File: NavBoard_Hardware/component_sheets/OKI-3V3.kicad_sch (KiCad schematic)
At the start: 4 parts, among them U4 OKI-3V3

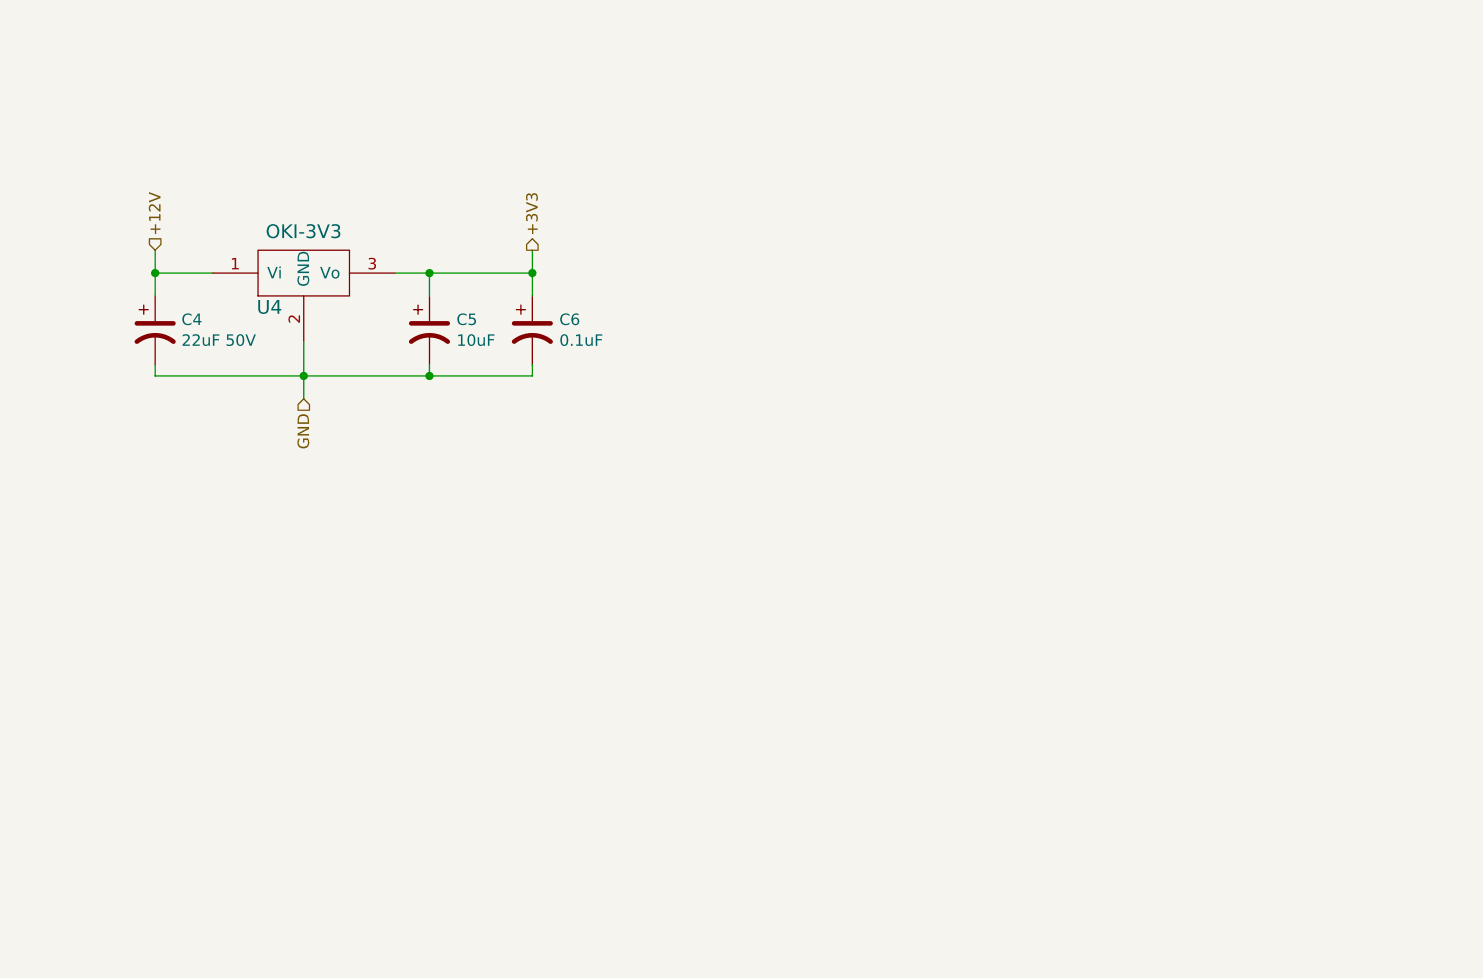
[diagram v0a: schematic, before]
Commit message: Added Information To Voltage Regulator Component Sheets, Improved Schematic Review 1 Powerpoint
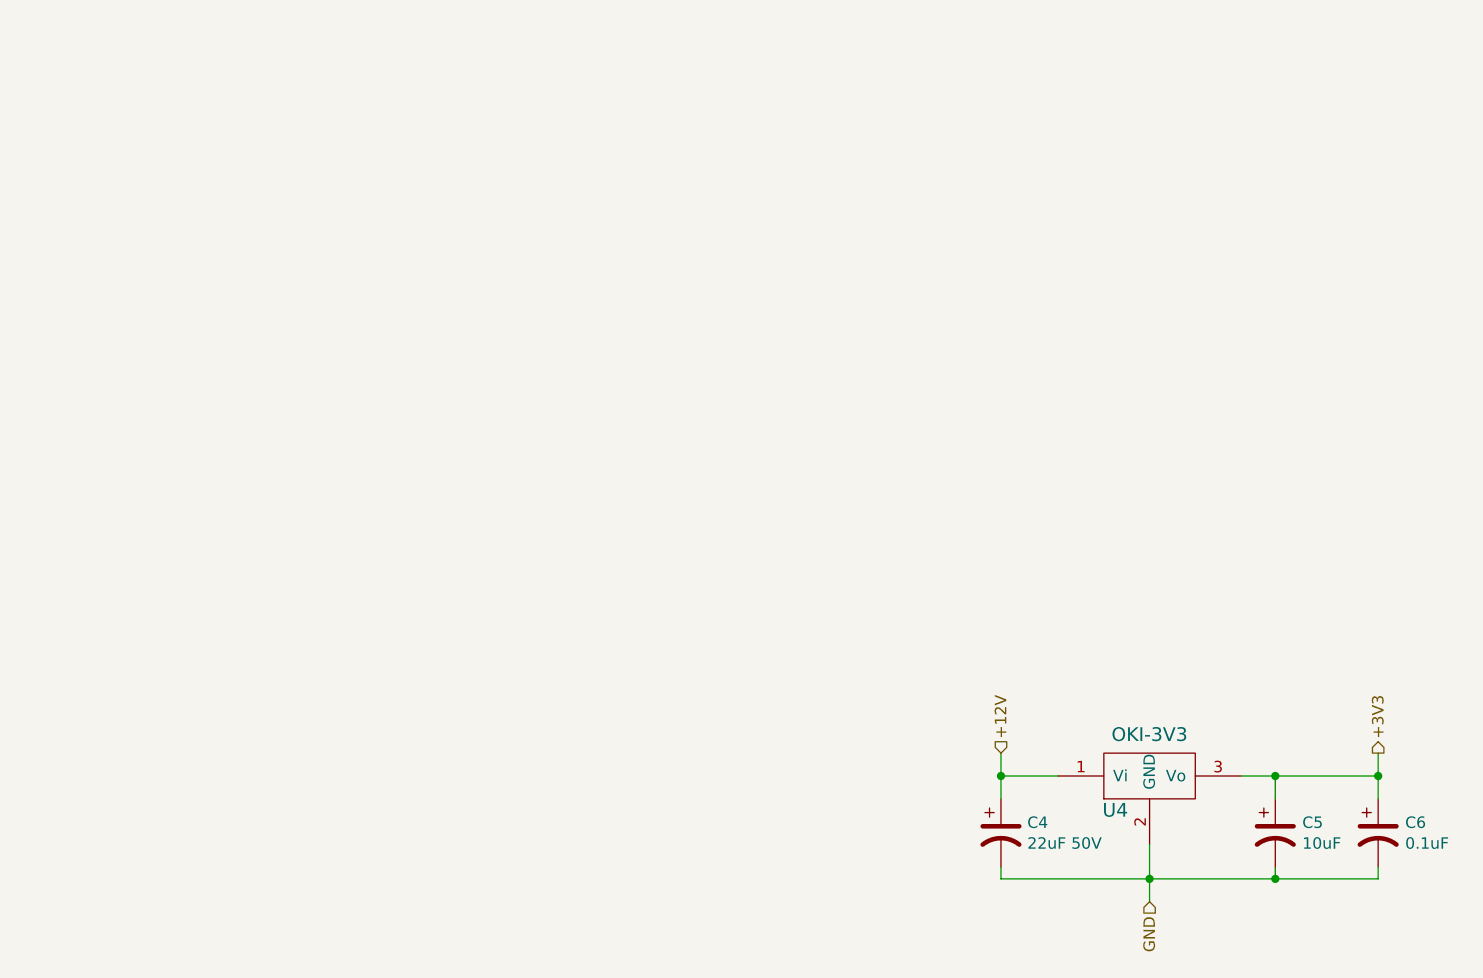
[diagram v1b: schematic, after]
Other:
- company: (none) -> Missouri S&T Mars Rover Design Team
- title: (none) -> OKI 3V3 Voltage Regulator
- moved on the sheet: C4, C5, C6, U4
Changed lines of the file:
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@@
 (kicad_sch (version 20211123) (generator eeschema)
   (paper "A4")
-  (junction (at 115.57 90.17) (diameter 0) (color 0 0 0 0)
+  (title_block
+    (title "OKI 3V3 Voltage Regulator")
+    (date "2022-09-17")
+    (rev "2, 2023")
+    (company "Missouri S&T Mars Rover Design Team")
+    (comment 1 "OKI 3V3 Voltage Regulator")
+    (comment 2 "Provides Stable 3V3 From 12V")
   )
-  (junction (at 157.48 90.17) (diameter 0) (color 0 0 0 0)
+  (junction (at 209.55 146.05) (diameter 0) (color 0 0 0 0)
   )
-  (junction (at 146.05 90.17) (diameter 0) (color 0 0 0 0)
+  (junction (at 251.46 146.05) (diameter 0) (color 0 0 0 0)
   )
-  (junction (at 146.05 101.6) (diameter 0) (color 0 0 0 0)
+  (junction (at 240.03 146.05) (diameter 0) (color 0 0 0 0)
   )
-  (junction (at 132.08 101.6) (diameter 0) (color 0 0 0 0)
+  (junction (at 240.03 157.48) (diameter 0) (color 0 0 0 0)
   )
-  (wire (pts (xy 146.05 101.6) (xy 157.48 101.6))
+  (junction (at 226.06 157.48) (diameter 0) (color 0 0 0 0)
+  )
+  (wire (pts (xy 240.03 157.48) (xy 251.46 157.48))
     (stroke (width 0) (type default) (color 0 0 0 0))
   )
-  (wire (pts (xy 132.08 101.6) (xy 146.05 101.6))
+  (wire (pts (xy 226.06 157.48) (xy 240.03 157.48))
     (stroke (width 0) (type default) (color 0 0 0 0))
   )
-  (wire (pts (xy 121.92 90.17) (xy 115.57 90.17))
+  (wire (pts (xy 215.9 146.05) (xy 209.55 146.05))
     (stroke (width 0) (type default) (color 0 0 0 0))
   )
-  (wire (pts (xy 146.05 101.6) (xy 146.05 100.33))
+  (wire (pts (xy 240.03 157.48) (xy 240.03 156.21))
     (stroke (width 0) (type default) (color 0 0 0 0))
   )
-  (wire (pts (xy 146.05 90.17) (xy 157.48 90.17))
+  (wire (pts (xy 240.03 146.05) (xy 251.46 146.05))
     (stroke (width 0) (type default) (color 0 0 0 0))
   )
-  (wire (pts (xy 132.08 97.79) (xy 132.08 101.6))
+  (wire (pts (xy 226.06 153.67) (xy 226.06 157.48))
     (stroke (width 0) (type default) (color 0 0 0 0))
   )
-  (wire (pts (xy 157.48 92.71) (xy 157.48 90.17))
+  (wire (pts (xy 251.46 148.59) (xy 251.46 146.05))
     (stroke (width 0) (type default) (color 0 0 0 0))
   )
-  (wire (pts (xy 157.48 90.17) (xy 157.48 87.63))
+  (wire (pts (xy 251.46 146.05) (xy 251.46 143.51))
     (stroke (width 0) (type default) (color 0 0 0 0))
   )
-  (wire (pts (xy 115.57 87.63) (xy 115.57 90.17))
+  (wire (pts (xy 209.55 143.51) (xy 209.55 146.05))
     (stroke (width 0) (type default) (color 0 0 0 0))
   )
-  (wire (pts (xy 142.24 90.17) (xy 146.05 90.17))
+  (wire (pts (xy 236.22 146.05) (xy 240.03 146.05))
     (stroke (width 0) (type default) (color 0 0 0 0))
   )
-  (wire (pts (xy 115.57 90.17) (xy 115.57 92.71))
+  (wire (pts (xy 209.55 146.05) (xy 209.55 148.59))
     (stroke (width 0) (type default) (color 0 0 0 0))
   )
-  (wire (pts (xy 115.57 101.6) (xy 132.08 101.6))
+  (wire (pts (xy 209.55 157.48) (xy 226.06 157.48))
     (stroke (width 0) (type default) (color 0 0 0 0))
   )
-  (wire (pts (xy 132.08 101.6) (xy 132.08 104.14))
+  (wire (pts (xy 226.06 157.48) (xy 226.06 160.02))
     (stroke (width 0) (type default) (color 0 0 0 0))
   )
-  (wire (pts (xy 146.05 92.71) (xy 146.05 90.17))
+  (wire (pts (xy 240.03 148.59) (xy 240.03 146.05))
     (stroke (width 0) (type default) (color 0 0 0 0))
   )
-  (wire (pts (xy 157.48 101.6) (xy 157.48 100.33))
+  (wire (pts (xy 251.46 157.48) (xy 251.46 156.21))
     (stroke (width 0) (type default) (color 0 0 0 0))
   )
-  (wire (pts (xy 115.57 100.33) (xy 115.57 101.6))
+  (wire (pts (xy 209.55 156.21) (xy 209.55 157.48))
     (stroke (width 0) (type default) (color 0 0 0 0))
   )
-  (hierarchical_label "GND" (shape input) (at 132.08 104.14 270)
+  (hierarchical_label "GND" (shape input) (at 226.06 160.02 270)
     (effects (font (size 1.27 1.27)) (justify right))
   )
-  (hierarchical_label "+3V3" (shape output) (at 157.48 87.63 90)
+  (hierarchical_label "+3V3" (shape output) (at 251.46 143.51 90)
     (effects (font (size 1.27 1.27)) (justify left))
   )
-  (hierarchical_label "+12V" (shape input) (at 115.57 87.63 90)
+  (hierarchical_label "+12V" (shape input) (at 209.55 143.51 90)
     (effects (font (size 1.27 1.27)) (justify left))
   )
-  (symbol (lib_id "MRDT_Devices:OKI") (at 127 92.71 0) (unit 1)
+  (symbol (lib_id "MRDT_Devices:OKI") (at 220.98 148.59 0) (unit 1)
     (in_bom yes) (on_board yes)
-    (property "Reference" "U4" (id 0) (at 128.27 93.98 0)
+    (property "Reference" "U4" (id 0) (at 222.25 149.86 0)
       (effects (font (size 1.524 1.524)))
     )
-    (property "Value" "OKI-3V3" (id 1) (at 132.08 85.5726 0)
+    (property "Value" "OKI-3V3" (id 1) (at 226.06 141.4526 0)
       (effects (font (size 1.524 1.524)))
     )
-    (property "Footprint" "MRDT_Devices:OKI_Horizontal" (id 2) (at 121.92 95.25 0)
+    (property "Footprint" "MRDT_Devices:OKI_Horizontal" (id 2) (at 215.9 151.13 0)
       (effects (font (size 1.524 1.524)) hide)
     )
-    (property "Datasheet" "" (id 3) (at 121.92 95.25 0)
+    (property "Datasheet" "" (id 3) (at 215.9 151.13 0)
       (effects (font (size 1.524 1.524)) hide)
     )
@@
     (pin "3")
   )
-  (symbol (lib_id "Device:C_Polarized_US") (at 115.57 96.52 0) (unit 1)
+  (symbol (lib_id "Device:C_Polarized_US") (at 209.55 152.4 0) (unit 1)
     (in_bom yes) (on_board yes)
-    (property "Reference" "C4" (id 0) (at 118.491 95.3516 0)
+    (property "Reference" "C4" (id 0) (at 212.471 151.2316 0)
       (effects (font (size 1.27 1.27)) (justify left))
     )
-    (property "Value" "22uF 50V" (id 1) (at 118.491 97.663 0)
+    (property "Value" "22uF 50V" (id 1) (at 212.471 153.543 0)
       (effects (font (size 1.27 1.27)) (justify left))
     )
-    (property "Footprint" "Capacitor_THT:CP_Radial_D6.3mm_P2.50mm" (id 2) (at 115.57 96.52 0)
+    (property "Footprint" "Capacitor_THT:CP_Radial_D6.3mm_P2.50mm" (id 2) (at 209.55 152.4 0)
       (effects (font (size 1.27 1.27)) hide)
     )
-    (property "Datasheet" "~" (id 3) (at 115.57 96.52 0)
+    (property "Datasheet" "~" (id 3) (at 209.55 152.4 0)
       (effects (font (size 1.27 1.27)) hide)
     )
@@
     (pin "2")
   )
-  (symbol (lib_id "Device:C_Polarized_US") (at 157.48 96.52 0) (unit 1)
+  (symbol (lib_id "Device:C_Polarized_US") (at 251.46 152.4 0) (unit 1)
     (in_bom yes) (on_board yes)
-    (property "Reference" "C6" (id 0) (at 160.4772 95.3516 0)
+    (property "Reference" "C6" (id 0) (at 254.4572 151.2316 0)
       (effects (font (size 1.27 1.27)) (justify left))
     )
-    (property "Value" "0.1uF" (id 1) (at 160.4772 97.663 0)
+    (property "Value" "0.1uF" (id 1) (at 254.4572 153.543 0)
       (effects (font (size 1.27 1.27)) (justify left))
     )
-    (property "Footprint" "Capacitor_SMD:C_0603_1608Metric_Pad1.08x0.95mm_HandSolder" (id 2) (at 157.48 96.52 0)
+    (property "Footprint" "Capacitor_SMD:C_0603_1608Metric_Pad1.08x0.95mm_HandSolder" (id 2) (at 251.46 152.4 0)
       (effects (font (size 1.27 1.27)) hide)
     )
-    (property "Datasheet" "~" (id 3) (at 157.48 96.52 0)
+    (property "Datasheet" "~" (id 3) (at 251.46 152.4 0)
       (effects (font (size 1.27 1.27)) hide)
     )
@@
     (pin "2")
   )
-  (symbol (lib_id "Device:C_Polarized_US") (at 146.05 96.52 0) (unit 1)
+  (symbol (lib_id "Device:C_Polarized_US") (at 240.03 152.4 0) (unit 1)
     (in_bom yes) (on_board yes)
-    (property "Reference" "C5" (id 0) (at 149.0472 95.3516 0)
+    (property "Reference" "C5" (id 0) (at 243.0272 151.2316 0)
       (effects (font (size 1.27 1.27)) (justify left))
     )
-    (property "Value" "10uF" (id 1) (at 149.0472 97.663 0)
+    (property "Value" "10uF" (id 1) (at 243.0272 153.543 0)
       (effects (font (size 1.27 1.27)) (justify left))
     )
-    (property "Footprint" "Capacitor_SMD:C_0603_1608Metric_Pad1.08x0.95mm_HandSolder" (id 2) (at 146.05 96.52 0)
+    (property "Footprint" "Capacitor_SMD:C_0603_1608Metric_Pad1.08x0.95mm_HandSolder" (id 2) (at 240.03 152.4 0)
       (effects (font (size 1.27 1.27)) hide)
     )
-    (property "Datasheet" "~" (id 3) (at 146.05 96.52 0)
+    (property "Datasheet" "~" (id 3) (at 240.03 152.4 0)
       (effects (font (size 1.27 1.27)) hide)
     )

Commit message: Updated sheet title info
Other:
- company: Missouri S&T Mars Rover Design Team -> Thomas Francois, Katherine Dunlap, Missouri S&T Mars Rover Design Team
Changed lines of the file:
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@@
     (date "2022-09-17")
     (rev "2, 2023")
-    (company "Missouri S&T Mars Rover Design Team")
+    (company "Thomas Francois, Katherine Dunlap, Missouri S&T Mars Rover Design Team")
     (comment 1 "OKI 3V3 Voltage Regulator")
     (comment 2 "Provides Stable 3V3 From 12V")
